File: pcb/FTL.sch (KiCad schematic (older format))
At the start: 62 parts, among them J1 USB-MINI-A, J10 Encoder, J11 Power, J2 Motor, J3 Motor, J4 Power, J5 HEADER2X10, J6 HEADER2X10, J7 HEADER2X8, J8 UART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

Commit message: Finished board, sent to fabrication
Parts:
- added J12, J13: HEADER1X1, symbol HEADER1X1
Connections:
- net labels removed: +12V
- wire segments 324 -> 327

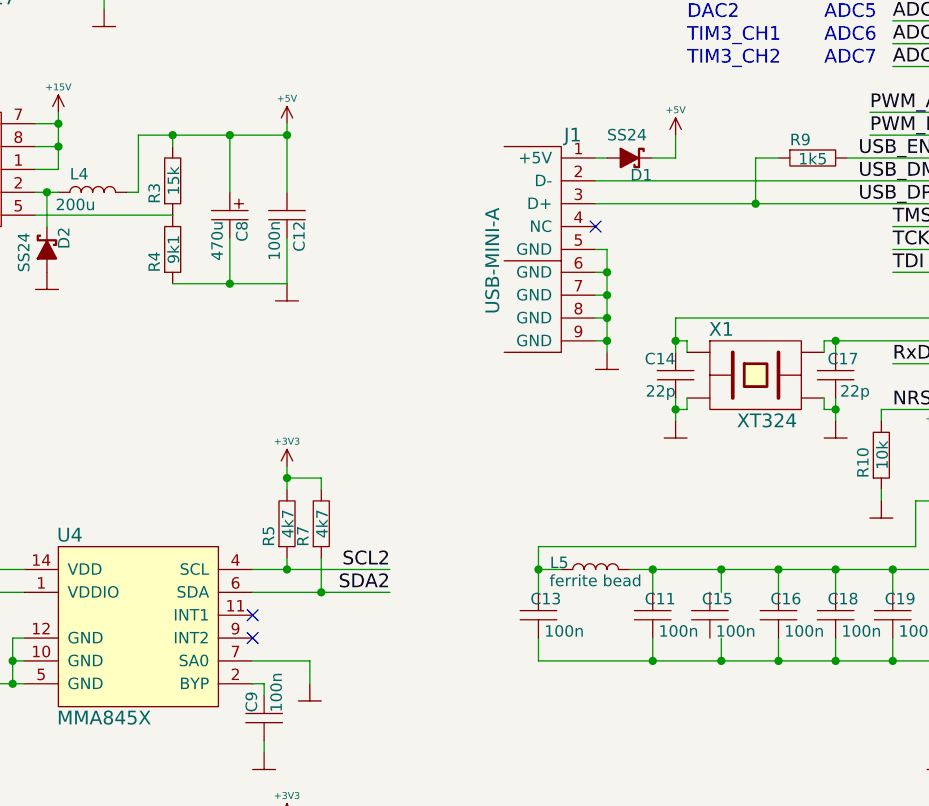
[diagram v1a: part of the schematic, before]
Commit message: Updated schematic, started firmware
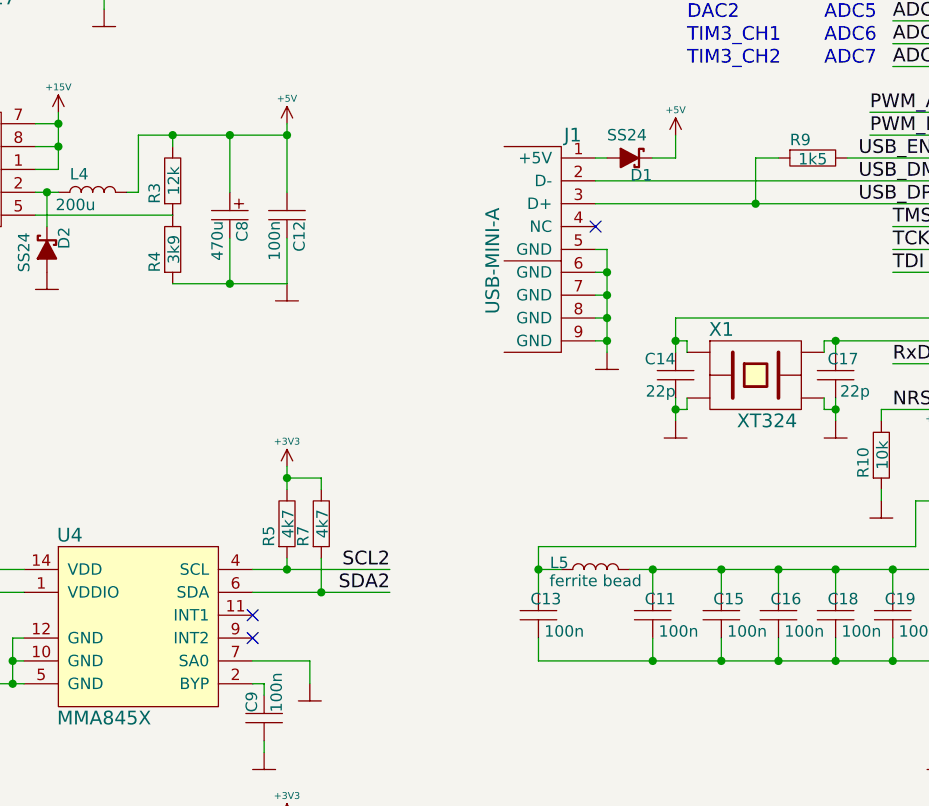
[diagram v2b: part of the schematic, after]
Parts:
- R3: value 15k -> 12k
- R4: value 9k1 -> 3k9
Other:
- moved on the sheet: C15
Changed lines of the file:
@@
-EESchema Schematic File Version 2  date pon, 21 sty 2013, 20:28:53
+EESchema Schematic File Version 2  date śro, 6 mar 2013, 13:58:31
 LIBS:newlib
 LIBS:power
@@
 Sheet 1 1
 Title "FTL"
-Date "21 jan 2013"
+Date "6 mar 2013"
 Rev "1"
 Comp "Zapol"
@@
 L C C15
 U 1 1 50CF80E4
-P 4750 3950
-F 0 "C15" V 4850 3850 50  0000 L BNN
-F 1 "100n" V 4650 3750 50  0000 L TNN
-	1    4750 3950
+P 4800 3950
+F 0 "C15" V 4900 3850 50  0000 L BNN
+F 1 "100n" V 4700 3750 50  0000 L TNN
+	1    4800 3950
 	0    -1   -1   0
 $EndComp
@@
 P 2400 2050
 F 0 "R3" H 2300 2100 50  0000 L BNN
-F 1 "15k" H 2400 2045 50  0000 C CNN
+F 1 "12k" H 2400 2045 50  0000 C CNN
 	1    2400 2050
 	0    -1   -1   0
@@
 P 2400 2350
 F 0 "R4" H 2300 2400 50  0000 L BNN
-F 1 "9k1" H 2400 2345 50  0000 C CNN
+F 1 "3k9" H 2400 2345 50  0000 C CNN
 	1    2400 2350
 	0    -1   -1   0

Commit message: Nie wiem co tu się zadziało... na wszelki wypadek robię commit
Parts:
- removed U7: STM32F103RXXX, symbol STM32F103RXXX
- added U?: STM32F103Rxxx, symbol STM32F103Rxxx
